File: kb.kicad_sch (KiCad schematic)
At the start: 1 part, among them U1 Pico

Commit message: started putting down symbols for matrix
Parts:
- added C? (x45): C_Small, symbol Device:C_Small
- added D? (x45): D_Small, symbol Device:D_Small
- added D? (x45): SK6812MINI, LED_SMD:LED_SK6812MINI_PLCC4_3.5x3.5mm_P1.75mm, symbol LED:SK6812MINI
- added MX? (x45): MX-NoLED, symbol MX_Alps_Hybrid:MX-NoLED
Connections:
- new net: D?.2 (A), MX?.2 (ROW) (x45)
- new net +5V: C?.1, C?.1, C?.1, C?.1, C?.1, C?.1, C?.1, C?.1, C?.1, C?.1, C?.1, C?.1, C?.1, C?.1, C?.1, C?.1, C?.1, C?.1, C?.1, C?.1, C?.1, C?.1, C?.1, C?.1, C?.1, C?.1, C?.1, C?.1, C?.1, C?.1, C?.1, C?.1, C?.1, C?.1, C?.1, C?.1, C?.1, C?.1, C?.1, C?.1, C?.1, C?.1, C?.1, C?.1, C?.1, D?.4 (VDD), D?.4 (VDD), D?.4 (VDD), D?.4 (VDD), D?.4 (VDD), D?.4 (VDD), D?.4 (VDD), D?.4 (VDD), D?.4 (VDD), D?.4 (VDD), D?.4 (VDD), D?.4 (VDD), D?.4 (VDD), D?.4 (VDD), D?.4 (VDD), D?.4 (VDD), D?.4 (VDD), D?.4 (VDD), D?.4 (VDD), D?.4 (VDD), D?.4 (VDD), D?.4 (VDD), D?.4 (VDD), D?.4 (VDD), D?.4 (VDD), D?.4 (VDD), D?.4 (VDD), D?.4 (VDD), D?.4 (VDD), D?.4 (VDD), D?.4 (VDD), D?.4 (VDD), D?.4 (VDD), D?.4 (VDD), D?.4 (VDD), D?.4 (VDD), D?.4 (VDD), D?.4 (VDD), D?.4 (VDD), D?.4 (VDD), D?.4 (VDD), D?.4 (VDD), D?.4 (VDD), D?.4 (VDD), D?.4 (VDD)
- new net GND: C?.2, C?.2, C?.2, C?.2, C?.2, C?.2, C?.2, C?.2, C?.2, C?.2, C?.2, C?.2, C?.2, C?.2, C?.2, C?.2, C?.2, C?.2, C?.2, C?.2, C?.2, C?.2, C?.2, C?.2, C?.2, C?.2, C?.2, C?.2, C?.2, C?.2, C?.2, C?.2, C?.2, C?.2, C?.2, C?.2, C?.2, C?.2, C?.2, C?.2, C?.2, C?.2, C?.2, C?.2, C?.2, D?.2 (VSS), D?.2 (VSS), D?.2 (VSS), D?.2 (VSS), D?.2 (VSS), D?.2 (VSS), D?.2 (VSS), D?.2 (VSS), D?.2 (VSS), D?.2 (VSS), D?.2 (VSS), D?.2 (VSS), D?.2 (VSS), D?.2 (VSS), D?.2 (VSS), D?.2 (VSS), D?.2 (VSS), D?.2 (VSS), D?.2 (VSS), D?.2 (VSS), D?.2 (VSS), D?.2 (VSS), D?.2 (VSS), D?.2 (VSS), D?.2 (VSS), D?.2 (VSS), D?.2 (VSS), D?.2 (VSS), D?.2 (VSS), D?.2 (VSS), D?.2 (VSS), D?.2 (VSS), D?.2 (VSS), D?.2 (VSS), D?.2 (VSS), D?.2 (VSS), D?.2 (VSS), D?.2 (VSS), D?.2 (VSS), D?.2 (VSS), D?.2 (VSS), D?.2 (VSS), D?.2 (VSS), D?.2 (VSS), D?.2 (VSS)

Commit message: started labelling nets
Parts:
- removed C?: C_Small, symbol Device:C_Small
- removed D?: D_Small, symbol Device:D_Small
- removed D?: SK6812MINI, LED_SMD:LED_SK6812MINI_PLCC4_3.5x3.5mm_P1.75mm, symbol LED:SK6812MINI
- removed MX?: MX-NoLED, symbol MX_Alps_Hybrid:MX-NoLED
- added D?: D_Small, symbol Device:D_Small
- added J?: Conn_01x04_Female, symbol Connector:Conn_01x04_Female
- added J?: HDMI_A, symbol Connector:HDMI_A
- added SW?: RotaryEncoder_Switch, symbol Device:RotaryEncoder_Switch
- added U?: SN74AHCT125D, SOIC127P600X175-14N, symbol SN74AHCT125D:SN74AHCT125D
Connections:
- net +5V: now also U1.40 (VBUS), J?.18 (+5V), J?.2 (Pin_2), U?.14 (VCC)
- net GND: now also U1.13 (GND), U1.18 (GND), U1.3 (GND), U1.42 (GND), U1.8 (GND), J?.1 (Pin_1), J?.17 (GND), SW?.C, U?.1 (1~{OE}), U?.10 (3~{OE}), U?.12 (4A), U?.13 (4~{OE}), U?.4 (2~{OE}), U?.5 (2A), U?.7 (GND), U?.9 (3A)
- net ROW2: now reaches D?.1 (K)
- net ROW2: now also D?.1 (K), D?.1 (K), D?.1 (K), D?.1 (K), D?.1 (K), D?.1 (K), D?.1 (K), D?.1 (K)
- net at D?.1 (DOUT): now also D?.3 (DIN) (x20)
- net at D?.3 (DIN): now also D?.1 (DOUT) (x19)
- net ROW1: now reaches D?.1 (K)
- net ROW1: now also D?.1 (K), D?.1 (K), D?.1 (K), D?.1 (K), D?.1 (K), D?.1 (K), D?.1 (K), D?.1 (K)
- net ROW3: now reaches D?.1 (K)
- net ROW3: now also D?.1 (K), D?.1 (K), D?.1 (K), D?.1 (K), D?.1 (K), D?.1 (K), D?.1 (K), D?.1 (K)
- net COL8: now reaches MX?.1 (COL)
- net COL8: now also MX?.1 (COL), MX?.1 (COL), MX?.1 (COL), MX?.1 (COL)
- net ROW4: now reaches D?.1 (K)
- net ROW4: now also D?.1 (K), D?.1 (K), D?.1 (K), D?.1 (K), D?.1 (K), D?.1 (K), D?.1 (K), D?.1 (K)
- net COL2: now reaches MX?.1 (COL)
- net COL2: now also MX?.1 (COL), MX?.1 (COL), MX?.1 (COL), MX?.1 (COL)
- net ROW0: now reaches D?.1 (K)
- net ROW0: now also D?.1 (K), D?.1 (K), D?.1 (K), D?.1 (K), D?.1 (K), D?.1 (K), D?.1 (K), D?.1 (K)
- net COL3: now reaches MX?.1 (COL)
- net COL3: now also MX?.1 (COL), MX?.1 (COL), MX?.1 (COL), MX?.1 (COL)
- net COL0: now reaches MX?.1 (COL)
- net COL0: now also MX?.1 (COL), MX?.1 (COL), MX?.1 (COL), SW?.S1
- net COL6: now reaches MX?.1 (COL)
- net COL6: now also MX?.1 (COL), MX?.1 (COL), MX?.1 (COL), MX?.1 (COL)
- net COL5: now reaches MX?.1 (COL)
- net COL5: now also MX?.1 (COL), MX?.1 (COL), MX?.1 (COL), MX?.1 (COL)
- net COL7: now reaches MX?.1 (COL)
- net COL7: now also MX?.1 (COL), MX?.1 (COL), MX?.1 (COL), MX?.1 (COL)
- net COL1: now reaches MX?.1 (COL)
- net COL1: now also MX?.1 (COL), MX?.1 (COL), MX?.1 (COL), MX?.1 (COL)
- net COL4: now reaches MX?.1 (COL)
- net COL4: now also MX?.1 (COL), MX?.1 (COL), MX?.1 (COL), MX?.1 (COL)
- new net: D?.2 (A), SW?.S2
- new net ENC_L1: SW?.A
- new net ENC_L2: SW?.B
- new net OLED_SCL: J?.3 (Pin_3)
- new net OLED_SDA: J?.4 (Pin_4)
- new net RGB_3V3: U?.2 (1A)
- new net RGB_5V: U?.3 (1Y)
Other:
- moved on the sheet: C?, D?, MX?, U1

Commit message: added footprints
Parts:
- removed J?: HDMI_A, symbol Connector:HDMI_A
- added J2: 10029449-001RLF, 10029449-001RLF:AMPHENOL_10029449-001RLF, symbol 10029449-001RLF:10029449-001RLF
- C1, C10, C11, C12, C13, C14, C15, C16, C17, C18, C19, C2, C20, C21, C22, C23, C24, C25, C26, C27, C28, C29, C3, C30, C31, C32, C33, C34, C35, C36, C37, C38, C39, C4, C40, C41, C42, C43, C44, C5, C6, C7, C8, C9: renamed from C?; footprint (none) -> Capacitor_SMD:C_0805_2012Metric_Pad1.18x1.45mm_HandSolder
- D1, D18, D19, D2, D20, D21, D22, D23, D24, D25, D26, D3, D36, D37, D38, D39, D4, D40, D41, D42, D43, D44, D5, D54, D55, D56, D57, D58, D59, D6, D60, D61, D62, D7, D72, D73, D74, D75, D76, D77, D78, D79, D8, D80: renamed from D?; footprint LED_SMD:LED_SK6812MINI_PLCC4_3.5x3.5mm_P1.75mm -> Keebio-Parts:SK6812-MINI-E
- D10, D11, D12, D13, D14, D15, D16, D17, D27, D28, D29, D30, D31, D32, D33, D34, D35, D45, D46, D47, D48, D49, D50, D51, D52, D53, D63, D64, D65, D66, D67, D68, D69, D70, D71, D81, D82, D83, D84, D85, D86, D87, D88, D89, D9: renamed from D?; footprint (none) -> Diode_SMD:D_SOD-123
- J1: renamed from J?; footprint (none) -> Connector_PinSocket_2.54mm:PinSocket_1x04_P2.54mm_Vertical
- MX1, MX10, MX11, MX13, MX14, MX15, MX16, MX17, MX18, MX19, MX2, MX20, MX22, MX23, MX24, MX25, MX26, MX27, MX28, MX29, MX3, MX31, MX32, MX33, MX34, MX35, MX36, MX37, MX38, MX4, MX44, MX5, MX6, MX7, MX8, MX9: renamed from MX?; footprint (none) -> MX_Only:MXOnly-1U-Hotswap
- MX12, MX39: renamed from MX?; footprint (none) -> MX_Only:MXOnly-1.5U-Hotswap
- MX21: renamed from MX?; footprint (none) -> MX_Only:MXOnly-1.75U-Hotswap
- MX30: renamed from MX?; footprint (none) -> MX_Only:MXOnly-2.25U-Hotswap
- MX40, MX41, MX42: renamed from MX?; footprint (none) -> MX_Only:MXOnly-1.25U-Hotswap
- MX43: renamed from MX?; footprint (none) -> MX_Only:MXOnly-2U-Hotswap
- SW1: renamed from SW?; footprint (none) -> Keebio-Parts:RotaryEncoder_EC11
- U2: renamed from U?; footprint SOIC127P600X175-14N -> Package_DIP:DIP-14_W7.62mm_Socket
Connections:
- net +5V: now also J2.18
- net GND: now also J2.17, J2.S1 (SHIELD), J2.S2 (SHIELD), J2.S3 (SHIELD), J2.S4 (SHIELD)

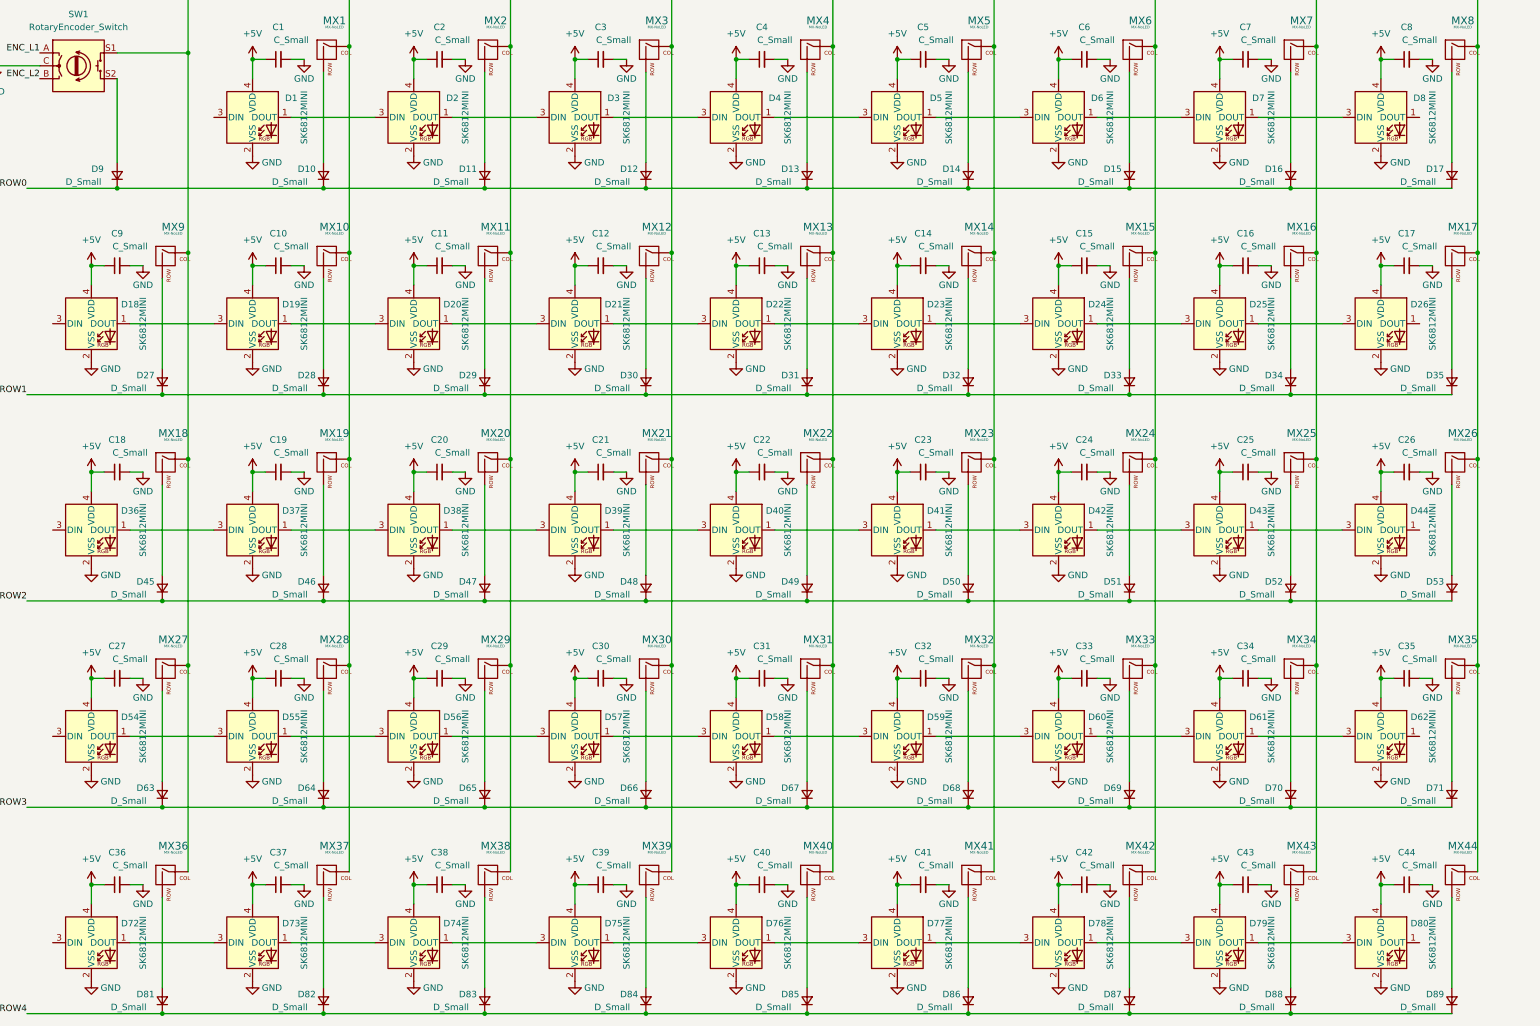
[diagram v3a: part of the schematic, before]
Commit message: fixed diode designators
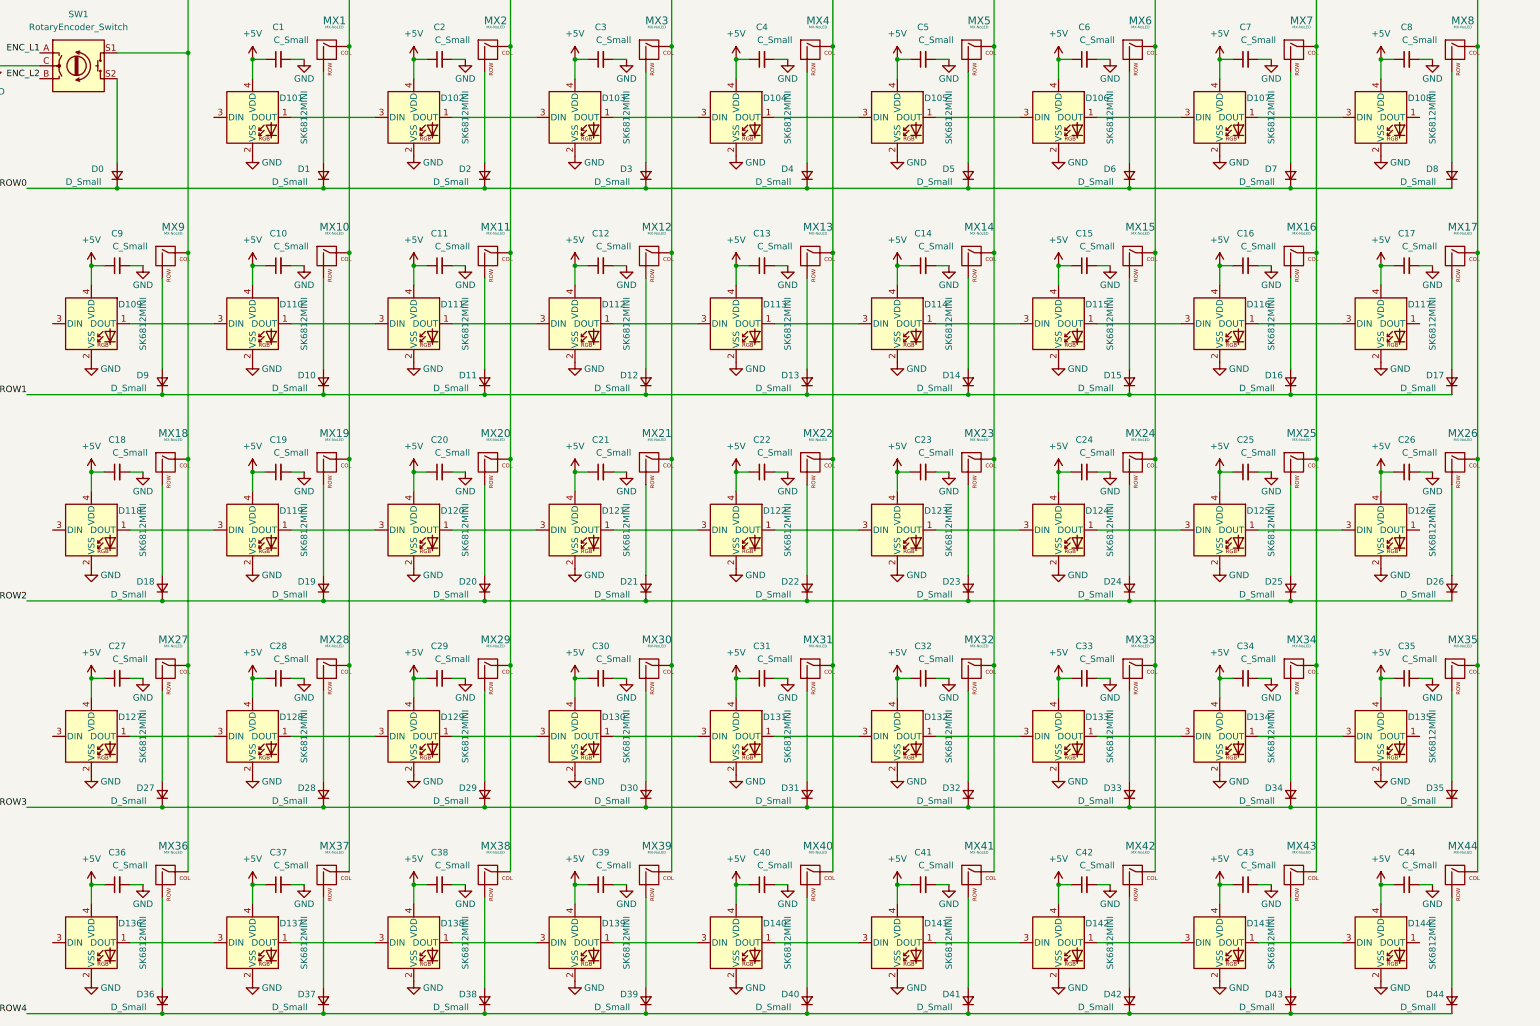
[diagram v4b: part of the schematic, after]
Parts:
- renumbered D9 to D0, D10 to D1, D28 to D10, D1 to D101, D2 to D102, D3 to D103, D4 to D104, D5 to D105, D6 to D106, D7 to D107, D8 to D108, D18 to D109, D29 to D11, D19 to D110, D20 to D111, D21 to D112, D22 to D113, D23 to D114, D24 to D115, D25 to D116, D26 to D117, D36 to D118, D37 to D119, D30 to D12, D38 to D120, D39 to D121, D40 to D122, D41 to D123, D42 to D124, D43 to D125, D44 to D126, D54 to D127, D55 to D128, D56 to D129, D31 to D13, D57 to D130, D58 to D131, D59 to D132, D60 to D133, D61 to D134, D62 to D135, D72 to D136, D73 to D137, D74 to D138, D75 to D139, D32 to D14, D76 to D140, D77 to D141, D78 to D142, D79 to D143, D80 to D144, D33 to D15, D34 to D16, D35 to D17, D45 to D18, D46 to D19, D11 to D2, D47 to D20, D48 to D21, D49 to D22, D50 to D23, D51 to D24, D52 to D25, D53 to D26, D63 to D27, D64 to D28, D65 to D29, D12 to D3, D66 to D30, D67 to D31, D68 to D32, D69 to D33, D70 to D34, D71 to D35, D81 to D36, D82 to D37, D83 to D38, D84 to D39, D13 to D4, D85 to D40, D86 to D41, D87 to D42, D88 to D43, D89 to D44, D14 to D5, D15 to D6, D16 to D7, D17 to D8, D27 to D9

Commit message: about to start routing
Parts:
- U2: footprint Package_DIP:DIP-14_W7.62mm_Socket -> Package_SO:TSSOP-14-1EP_4.4x5mm_P0.65mm
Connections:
- net RGB_5V: now also D101.3 (DIN)
- net at D135.1 (DOUT): now also D136.3 (DIN)
- net at D108.1 (DOUT): now also D109.3 (DIN)
- net at D126.1 (DOUT): now also D127.3 (DIN)
- net RGB_TO_RIGHT: now reaches D144.1 (DOUT)
- net at D118.3 (DIN): now also D117.1 (DOUT)
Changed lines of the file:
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@@
     (stroke (width 0) (type default) (color 0 0 0 0))
   )
+  (wire (pts (xy 299.72 93.98) (xy 316.23 93.98))
+    (stroke (width 0) (type default) (color 0 0 0 0))
+  )
   (wire (pts (xy 133.35 204.47) (xy 135.89 204.47))
     (stroke (width 0) (type default) (color 0 0 0 0))
   )
+  (wire (pts (xy 316.23 134.62) (xy 316.23 151.13))
+    (stroke (width 0) (type default) (color 0 0 0 0))
+  )
   (wire (pts (xy 299.72 245.11) (xy 302.26 245.11))
     (stroke (width 0) (type default) (color 0 0 0 0))
@@
     (stroke (width 0) (type default) (color 0 0 0 0))
   )
+  (wire (pts (xy 316.23 93.98) (xy 316.23 110.49))
+    (stroke (width 0) (type default) (color 0 0 0 0))
+  )
+  (wire (pts (xy 26.67 151.13) (xy 26.67 175.26))
+    (stroke (width 0) (type default) (color 0 0 0 0))
+  )
   (wire (pts (xy 204.47 163.83) (xy 207.01 163.83))
     (stroke (width 0) (type default) (color 0 0 0 0))
@@
     (stroke (width 0) (type default) (color 0 0 0 0))
   )
+  (wire (pts (xy 299.72 134.62) (xy 316.23 134.62))
+    (stroke (width 0) (type default) (color 0 0 0 0))
+  )
   (wire (pts (xy 267.97 175.26) (xy 284.48 175.26))
     (stroke (width 0) (type default) (color 0 0 0 0))
@@
     (stroke (width 0) (type default) (color 0 0 0 0))
   )
+  (wire (pts (xy 299.72 215.9) (xy 316.23 215.9))
+    (stroke (width 0) (type default) (color 0 0 0 0))
+  )
   (wire (pts (xy 25.4 107.95) (xy 43.18 107.95))
     (stroke (width 0) (type default) (color 0 0 0 0))
@@
     (stroke (width 0) (type default) (color 0 0 0 0))
   )
+  (wire (pts (xy 26.67 232.41) (xy 26.67 256.54))
+    (stroke (width 0) (type default) (color 0 0 0 0))
+  )
   (wire (pts (xy 292.1 82.55) (xy 292.1 86.36))
     (stroke (width 0) (type default) (color 0 0 0 0))
@@
     (stroke (width 0) (type default) (color 0 0 0 0))
   )
+  (wire (pts (xy 316.23 232.41) (xy 26.67 232.41))
+    (stroke (width 0) (type default) (color 0 0 0 0))
+  )
   (wire (pts (xy 147.32 229.87) (xy 179.07 229.87))
     (stroke (width 0) (type default) (color 0 0 0 0))
@@
     (stroke (width 0) (type default) (color 0 0 0 0))
   )
+  (wire (pts (xy 316.23 151.13) (xy 26.67 151.13))
+    (stroke (width 0) (type default) (color 0 0 0 0))
+  )
   (wire (pts (xy 69.85 245.11) (xy 72.39 245.11))
     (stroke (width 0) (type default) (color 0 0 0 0))
@@
     (stroke (width 0) (type default) (color 0 0 0 0))
   )
+  (wire (pts (xy 316.23 191.77) (xy 26.67 191.77))
+    (stroke (width 0) (type default) (color 0 0 0 0))
+  )
   (wire (pts (xy 38.1 163.83) (xy 40.64 163.83))
     (stroke (width 0) (type default) (color 0 0 0 0))
@@
     (stroke (width 0) (type default) (color 0 0 0 0))
   )
+  (wire (pts (xy 26.67 215.9) (xy 30.48 215.9))
+    (stroke (width 0) (type default) (color 0 0 0 0))
+  )
   (wire (pts (xy 267.97 215.9) (xy 284.48 215.9))
     (stroke (width 0) (type default) (color 0 0 0 0))
@@
     (stroke (width 0) (type default) (color 0 0 0 0))
   )
+  (wire (pts (xy 26.67 256.54) (xy 30.48 256.54))
+    (stroke (width 0) (type default) (color 0 0 0 0))
+  )
   (wire (pts (xy 83.82 85.09) (xy 83.82 102.87))
     (stroke (width 0) (type default) (color 0 0 0 0))
@@
     (stroke (width 0) (type default) (color 0 0 0 0))
   )
+  (wire (pts (xy 26.67 175.26) (xy 30.48 175.26))
+    (stroke (width 0) (type default) (color 0 0 0 0))
+  )
   (wire (pts (xy 140.97 93.98) (xy 157.48 93.98))
     (stroke (width 0) (type default) (color 0 0 0 0))
@@
     (stroke (width 0) (type default) (color 0 0 0 0))
   )
+  (wire (pts (xy 316.23 175.26) (xy 316.23 191.77))
+    (stroke (width 0) (type default) (color 0 0 0 0))
+  )
   (wire (pts (xy 274.32 125.73) (xy 274.32 143.51))
     (stroke (width 0) (type default) (color 0 0 0 0))
@@
     (stroke (width 0) (type default) (color 0 0 0 0))
   )
+  (wire (pts (xy 299.72 175.26) (xy 316.23 175.26))
+    (stroke (width 0) (type default) (color 0 0 0 0))
+  )
   (wire (pts (xy 210.82 189.23) (xy 242.57 189.23))
     (stroke (width 0) (type default) (color 0 0 0 0))
@@
     (stroke (width 0) (type default) (color 0 0 0 0))
   )
+  (wire (pts (xy 26.67 110.49) (xy 26.67 134.62))
+    (stroke (width 0) (type default) (color 0 0 0 0))
+  )
+  (wire (pts (xy 26.67 191.77) (xy 26.67 215.9))
+    (stroke (width 0) (type default) (color 0 0 0 0))
+  )
   (wire (pts (xy 83.82 270.51) (xy 115.57 270.51))
     (stroke (width 0) (type default) (color 0 0 0 0))
@@
     (stroke (width 0) (type default) (color 0 0 0 0))
   )
+  (wire (pts (xy 299.72 256.54) (xy 311.15 256.54))
+    (stroke (width 0) (type default) (color 0 0 0 0))
+  )
   (wire (pts (xy 242.57 189.23) (xy 274.32 189.23))
     (stroke (width 0) (type default) (color 0 0 0 0))
@@
     (stroke (width 0) (type default) (color 0 0 0 0))
   )
+  (wire (pts (xy 26.67 134.62) (xy 30.48 134.62))
+    (stroke (width 0) (type default) (color 0 0 0 0))
+  )
   (wire (pts (xy 77.47 256.54) (xy 93.98 256.54))
     (stroke (width 0) (type default) (color 0 0 0 0))
@@
     (stroke (width 0) (type default) (color 0 0 0 0))
   )
+  (wire (pts (xy 316.23 215.9) (xy 316.23 232.41))
+    (stroke (width 0) (type default) (color 0 0 0 0))
+  )
   (wire (pts (xy 115.57 166.37) (xy 115.57 184.15))
     (stroke (width 0) (type default) (color 0 0 0 0))
@@
     (stroke (width 0) (type default) (color 0 0 0 0))
   )
+  (wire (pts (xy 316.23 110.49) (xy 26.67 110.49))
+    (stroke (width 0) (type default) (color 0 0 0 0))
+  )
   (label "COL2" (at 120.65 67.31 90)
     (effects (font (size 1.27 1.27)) (justify left bottom))
@@
     (effects (font (size 1.27 1.27)) (justify right bottom))
   )
+  (label "RGB_TO_RIGHT" (at 311.15 256.54 0)
+    (effects (font (size 1.27 1.27)) (justify left bottom))
+  )
   (label "ROW2" (at 25.4 189.23 180)
     (effects (font (size 1.27 1.27)) (justify right bottom))
@@
     (effects (font (size 1.27 1.27)) (justify left bottom))
   )
+  (label "RGB_5V" (at 62.23 93.98 180)
+    (effects (font (size 1.27 1.27)) (justify right bottom))
+  )
   (label "OLED_SCL" (at 213.36 31.75 180)
     (effects (font (size 1.27 1.27)) (justify right bottom))
@@
     (property "Reference" "U2" (id 0) (at 137.16 13.97 0))
     (property "Value" "SN74AHCT125D" (id 1) (at 137.16 16.51 0))
-    (property "Footprint" "Package_DIP:DIP-14_W7.62mm_Socket" (id 2) (at 137.16 36.83 0)
+    (property "Footprint" "Package_SO:TSSOP-14-1EP_4.4x5mm_P0.65mm" (id 2) (at 137.16 36.83 0)
       (effects (font (size 1.27 1.27)) (justify left bottom) hide)
     )
@@
     (pin "1")
   )
+  (symbol (lib_id "MCU_RaspberryPi_and_Boards:Pico") (at 50.8 36.83 90) (unit 1)
+    (in_bom yes) (on_board yes) (fields_autoplaced)
+    (property "Reference" "U1" (id 0) (at 22.86 35.5599 90)
+      (effects (font (size 1.27 1.27)) (justify left))
+    )
+    (property "Value" "Pico" (id 1) (at 22.86 38.0999 90)
+      (effects (font (size 1.27 1.27)) (justify left))
+    )
+    (property "Footprint" "MCU_RaspberryPi_and_Boards:RPi_Pico_SMD_TH" (id 2) (at 50.8 36.83 90)
+      (effects (font (size 1.27 1.27)) hide)
+    )
+    (property "Datasheet" "" (id 3) (at 50.8 36.83 0)
+      (effects (font (size 1.27 1.27)) hide)
+    )
+    (pin "1")
+    (pin "10")
+    (pin "11")
+    (pin "12")
+    (pin "13")
+    (pin "14")
+    (pin "15")
+    (pin "16")
+    (pin "17")
+    (pin "18")
+    (pin "19")
+    (pin "2")
+    (pin "20")
+    (pin "21")
+    (pin "22")
+    (pin "23")
+    (pin "24")
+    (pin "25")
+    (pin "26")
+    (pin "27")
+    (pin "28")
+    (pin "29")
+    (pin "3")
+    (pin "30")
+    (pin "31")
+    (pin "32")
+    (pin "33")
+    (pin "34")
+    (pin "35")
+    (pin "36")
+    (pin "37")
+    (pin "38")
+    (pin "39")
+    (pin "4")
+    (pin "40")
+    (pin "41")
+    (pin "42")
+    (pin "43")
+    (pin "5")
+    (pin "6")
+    (pin "7")
+    (pin "8")
+    (pin "9")
+  )
   (symbol (lib_id "Device:C_Small") (at 233.68 204.47 90) (unit 1)
     (in_bom yes) (on_board yes)
@@
     (pin "2")
   )
-  (symbol (lib_id "MCU_RaspberryPi_and_Boards:Pico") (at 50.8 36.83 90) (unit 1)
-    (in_bom yes) (on_board yes) (fields_autoplaced)
-    (property "Reference" "U1" (id 0) (at 22.86 35.5599 90)
-      (effects (font (size 1.27 1.27)) (justify left))
-    )
-    (property "Value" "Pico" (id 1) (at 22.86 38.0999 90)
-      (effects (font (size 1.27 1.27)) (justify left))
-    )
-    (property "Footprint" "MCU_RaspberryPi_and_Boards:RPi_Pico_SMD_TH" (id 2) (at 50.8 36.83 90)
-      (effects (font (size 1.27 1.27)) hide)
-    )
-    (property "Datasheet" "" (id 3) (at 50.8 36.83 0)
-      (effects (font (size 1.27 1.27)) hide)
-    )
-    (pin "1")
-    (pin "10")
-    (pin "11")
-    (pin "12")
-    (pin "13")
-    (pin "14")
-    (pin "15")
-    (pin "16")
-    (pin "17")
-    (pin "18")
-    (pin "19")
-    (pin "2")
-    (pin "20")
-    (pin "21")
-    (pin "22")
-    (pin "23")
-    (pin "24")
-    (pin "25")
-    (pin "26")
-    (pin "27")
-    (pin "28")
-    (pin "29")
-    (pin "3")
-    (pin "30")
-    (pin "31")
-    (pin "32")
-    (pin "33")
-    (pin "34")
-    (pin "35")
-    (pin "36")
-    (pin "37")
-    (pin "38")
-    (pin "39")
-    (pin "4")
-    (pin "40")
-    (pin "41")
-    (pin "42")
-    (pin "43")
-    (pin "5")
-    (pin "6")
-    (pin "7")
-    (pin "8")
-    (pin "9")
-  )
   (symbol (lib_id "Device:C_Small") (at 265.43 123.19 90) (unit 1)
     (in_bom yes) (on_board yes)
@@
       (reference "SW1") (unit 1) (value "RotaryEncoder_Switch") (footprint "Keebio-Parts:RotaryEncoder_EC11")
     )
-    (path "/d2a576d9-55f6-4c4d-b69b-1cbcc0583c5f"
+    (path "/a7cbddcd-1e50-487a-a96f-08c94a194de5"
       (reference "U1") (unit 1) (value "Pico") (footprint "MCU_RaspberryPi_and_Boards:RPi_Pico_SMD_TH")
     )
     (path "/5a89d915-3452-4935-b466-ffb2e72f4cd0"
-      (reference "U2") (unit 1) (value "SN74AHCT125D") (footprint "Package_DIP:DIP-14_W7.62mm_Socket")
+      (reference "U2") (unit 1) (value "SN74AHCT125D") (footprint "Package_SO:TSSOP-14-1EP_4.4x5mm_P0.65mm")
     )
   )
